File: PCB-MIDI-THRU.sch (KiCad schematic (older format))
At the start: 61 parts, among them J1 Conn_02x05_Odd_Even, J2 Conn_01x02_Male, J3 Conn_01x02_Male, J4 Conn_01x02_Male, J5 Conn_01x02_Male, J6 Conn_01x02_Male, J7 Conn_01x02_Male, U1 L7805, U2 6N136, U3 74LS14

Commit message: v0.0.1 PCB SCHEM
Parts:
- added C9: C, Capacitor_THT:C_Disc_D4.3mm_W1.9mm_P5.00mm, symbol Device:C
- C2, C3, C4, C5, C6, C7, C8: footprint (none) -> Capacitor_THT:CP_Radial_D5.0mm_P2.50mm
- U1: footprint (none) -> Package_TO_SOT_THT:TO-220-3_Horizontal_TabDown
- U2: footprint (none) -> Package_DIP:DIP-8_W7.62mm
- U3: footprint (none) -> Package_DIP:DIP-14_W7.62mm
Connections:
- net +5V: now also C9.1
- net GND: now also C9.2
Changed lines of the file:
@@
 F 0 "U2" H 3250 1975 50  0000 C CNN
 F 1 "6N136" H 3250 1884 50  0000 C CNN
-F 2 "" H 3050 1250 50  0001 L CIN
+F 2 "Package_DIP:DIP-8_W7.62mm" H 3050 1250 50  0001 L CIN
 F 3 "http://www.ti.com/lit/gpn/sn74LS14" H 3250 1550 50  0001 L CNN
 	1    3250 1550
@@
 F 0 "U3" H 5050 1967 50  0000 C CNN
 F 1 "74LS14" H 5050 1876 50  0000 C CNN
-F 2 "" H 5050 1650 50  0001 C CNN
+F 2 "Package_DIP:DIP-14_W7.62mm" H 5050 1650 50  0001 C CNN
 F 3 "http://www.ti.com/lit/gpn/sn74LS14" H 5050 1650 50  0001 C CNN
 	1    5050 1650
@@
 F 0 "U3" H 6350 2367 50  0000 C CNN
 F 1 "74LS14" H 6350 2276 50  0000 C CNN
-F 2 "" H 6350 2050 50  0001 C CNN
+F 2 "Package_DIP:DIP-14_W7.62mm" H 6350 2050 50  0001 C CNN
 F 3 "http://www.ti.com/lit/gpn/sn74LS14" H 6350 2050 50  0001 C CNN
 	2    6350 2050
@@
 F 0 "U3" H 6350 2917 50  0000 C CNN
 F 1 "74LS14" H 6350 2826 50  0000 C CNN
-F 2 "" H 6350 2600 50  0001 C CNN
+F 2 "Package_DIP:DIP-14_W7.62mm" H 6350 2600 50  0001 C CNN
 F 3 "http://www.ti.com/lit/gpn/sn74LS14" H 6350 2600 50  0001 C CNN
 	3    6350 2600
@@
 F 0 "U3" H 6350 3517 50  0000 C CNN
 F 1 "74LS14" H 6350 3426 50  0000 C CNN
-F 2 "" H 6350 3200 50  0001 C CNN
+F 2 "Package_DIP:DIP-14_W7.62mm" H 6350 3200 50  0001 C CNN
 F 3 "http://www.ti.com/lit/gpn/sn74LS14" H 6350 3200 50  0001 C CNN
 	4    6350 3200
@@
 F 0 "U3" H 6350 4117 50  0000 C CNN
 F 1 "74LS14" H 6350 4026 50  0000 C CNN
-F 2 "" H 6350 3800 50  0001 C CNN
+F 2 "Package_DIP:DIP-14_W7.62mm" H 6350 3800 50  0001 C CNN
 F 3 "http://www.ti.com/lit/gpn/sn74LS14" H 6350 3800 50  0001 C CNN
 	6    6350 3800
@@
 F 0 "U3" H 3730 4196 50  0000 L CNN
 F 1 "74LS14" H 3730 4105 50  0000 L CNN
-F 2 "" H 3500 4150 50  0001 C CNN
+F 2 "Package_DIP:DIP-14_W7.62mm" H 3500 4150 50  0001 C CNN
 F 3 "http://www.ti.com/lit/gpn/sn74LS14" H 3500 4150 50  0001 C CNN
 	7    3500 4150
@@
 F 0 "U1" H 2400 3942 50  0000 C CNN
 F 1 "L7805" H 2400 3851 50  0000 C CNN
-F 2 "" H 2425 3550 50  0001 L CIN
+F 2 "Package_TO_SOT_THT:TO-220-3_Horizontal_TabDown" H 2425 3550 50  0001 L CIN
 F 3 "http://www.st.com/content/ccc/resource/technical/document/datasheet/41/4f/b3/b0/12/d4/47/88/CD00000444.pdf/files/CD00000444.pdf/jcr:content/translations/en.CD00000444.pdf" H 2400 3650 50  0001 C CNN
 	1    2400 3700
@@
 F 0 "C2" H 2788 4096 50  0000 L CNN
 F 1 "10UF" H 2788 4005 50  0000 L CNN
-F 2 "" H 2700 4050 50  0001 C CNN
+F 2 "Capacitor_THT:CP_Radial_D5.0mm_P2.50mm" H 2700 4050 50  0001 C CNN
 F 3 "~" H 2700 4050 50  0001 C CNN
 	1    2700 4050
@@
 F 0 "U3" H 6350 4717 50  0000 C CNN
 F 1 "74LS14" H 6350 4626 50  0000 C CNN
-F 2 "" H 6350 4400 50  0001 C CNN
+F 2 "Package_DIP:DIP-14_W7.62mm" H 6350 4400 50  0001 C CNN
 F 3 "http://www.ti.com/lit/gpn/sn74LS14" H 6350 4400 50  0001 C CNN
 	5    6350 4400
@@
 F 0 "C4" V 9950 2250 50  0000 C CNN
 F 1 "10UF" V 9950 2600 50  0000 C CNN
-F 2 "" H 10000 2400 50  0001 C CNN
+F 2 "Capacitor_THT:CP_Radial_D5.0mm_P2.50mm" H 10000 2400 50  0001 C CNN
 F 3 "~" H 10000 2400 50  0001 C CNN
 	1    10000 2400
@@
 F 0 "C5" V 9950 2800 50  0000 C CNN
 F 1 "10UF" V 9950 3150 50  0000 C CNN
-F 2 "" H 10000 2950 50  0001 C CNN
+F 2 "Capacitor_THT:CP_Radial_D5.0mm_P2.50mm" H 10000 2950 50  0001 C CNN
 F 3 "~" H 10000 2950 50  0001 C CNN
 	1    10000 2950
@@
 F 0 "C6" V 9950 3450 50  0000 C CNN
 F 1 "10UF" V 9950 3800 50  0000 C CNN
-F 2 "" H 10000 3600 50  0001 C CNN
+F 2 "Capacitor_THT:CP_Radial_D5.0mm_P2.50mm" H 10000 3600 50  0001 C CNN
 F 3 "~" H 10000 3600 50  0001 C CNN
 	1    10000 3600
@@
 F 0 "C7" V 9950 4000 50  0000 C CNN
 F 1 "10UF" V 9950 4350 50  0000 C CNN
-F 2 "" H 10000 4150 50  0001 C CNN
+F 2 "Capacitor_THT:CP_Radial_D5.0mm_P2.50mm" H 10000 4150 50  0001 C CNN
 F 3 "~" H 10000 4150 50  0001 C CNN
 	1    10000 4150
@@
 F 0 "C8" V 9950 4600 50  0000 C CNN
 F 1 "10UF" V 9950 4950 50  0000 C CNN
-F 2 "" H 10000 4750 50  0001 C CNN
+F 2 "Capacitor_THT:CP_Radial_D5.0mm_P2.50mm" H 10000 4750 50  0001 C CNN
 F 3 "~" H 10000 4750 50  0001 C CNN
 	1    10000 4750
@@
 F 0 "C3" V 5600 2200 50  0000 C CNN
 F 1 "10UF" V 5600 2550 50  0000 C CNN
-F 2 "" H 5650 2350 50  0001 C CNN
+F 2 "Capacitor_THT:CP_Radial_D5.0mm_P2.50mm" H 5650 2350 50  0001 C CNN
 F 3 "~" H 5650 2350 50  0001 C CNN
 	1    5650 2350
@@
 Text Notes 7500 6800 0    50   ~ 0
 MIDI THRU V0.0.1
+$Comp
+L Device:C C9
+U 1 1 60331913
+P 4150 4150
+F 0 "C9" H 4265 4196 50  0000 L CNN
+F 1 "C" H 4265 4105 50  0000 L CNN
+F 2 "Capacitor_THT:C_Disc_D4.3mm_W1.9mm_P5.00mm" H 4188 4000 50  0001 C CNN
+F 3 "~" H 4150 4150 50  0001 C CNN
+	1    4150 4150
+	1    0    0    -1
+$EndComp
+Wire Wire Line
+	4150 3650 4150 4000
+Wire Wire Line
+	3500 3650 4150 3650
+Connection ~ 3500 3650
+Wire Wire Line
+	3500 4650 4150 4650
+Wire Wire Line
+	4150 4650 4150 4300
+Connection ~ 3500 4650
 $EndSCHEMATC

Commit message: v0.0.1 Front
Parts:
- C9: value C -> 0.1uf
- D10, D11, D5, D7, D8, D9: value 1N4001 -> 1N4148
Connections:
- net at D1.1 (K), U1.1 (IN): now also C1.1, D2.1 (K)
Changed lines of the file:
@@
 $EndComp
 Wire Wire Line
-	1900 3700 2100 3700
+	1900 3700 2050 3700
 Wire Wire Line
 	2700 3700 2900 3700
@@
 	2200 3300 2050 3300
 Wire Wire Line
-	2050 3300 2050 3950
+	2050 3300 2050 3700
 Wire Wire Line
 	2700 4150 2400 4150
@@
 P 8950 2350
 F 0 "D7" H 8850 2300 50  0000 C CNN
-F 1 "1N4001" H 9150 2400 50  0000 C CNN
+F 1 "1N4148" H 9150 2400 50  0000 C CNN
 F 2 "Diode_THT:D_A-405_P10.16mm_Horizontal" H 8950 2225 50  0001 C CNN
 F 3 "~" H 8950 2350 50  0001 C CNN
@@
 P 8950 2900
 F 0 "D8" H 8850 2850 50  0000 C CNN
-F 1 "1N4001" H 9150 2950 50  0000 C CNN
+F 1 "1N4148" H 9150 2950 50  0000 C CNN
 F 2 "Diode_THT:D_A-405_P10.16mm_Horizontal" H 8950 2775 50  0001 C CNN
 F 3 "~" H 8950 2900 50  0001 C CNN
@@
 P 8950 3550
 F 0 "D9" H 8850 3500 50  0000 C CNN
-F 1 "1N4001" H 9150 3600 50  0000 C CNN
+F 1 "1N4148" H 9150 3600 50  0000 C CNN
 F 2 "Diode_THT:D_A-405_P10.16mm_Horizontal" H 8950 3425 50  0001 C CNN
 F 3 "~" H 8950 3550 50  0001 C CNN
@@
 P 8950 4100
 F 0 "D10" H 8850 4050 50  0000 C CNN
-F 1 "1N4001" H 9150 4150 50  0000 C CNN
+F 1 "1N4148" H 9150 4150 50  0000 C CNN
 F 2 "Diode_THT:D_A-405_P10.16mm_Horizontal" H 8950 3975 50  0001 C CNN
 F 3 "~" H 8950 4100 50  0001 C CNN
@@
 P 8950 4700
 F 0 "D11" H 8850 4650 50  0000 C CNN
-F 1 "1N4001" H 9150 4750 50  0000 C CNN
+F 1 "1N4148" H 9150 4750 50  0000 C CNN
 F 2 "Diode_THT:D_A-405_P10.16mm_Horizontal" H 8950 4575 50  0001 C CNN
 F 3 "~" H 8950 4700 50  0001 C CNN
@@
 P 4600 2300
 F 0 "D5" H 4500 2250 50  0000 C CNN
-F 1 "1N4001" H 4800 2350 50  0000 C CNN
+F 1 "1N4148" H 4800 2350 50  0000 C CNN
 F 2 "Diode_THT:D_A-405_P10.16mm_Horizontal" H 4600 2175 50  0001 C CNN
 F 3 "~" H 4600 2300 50  0001 C CNN
@@
 P 4150 4150
 F 0 "C9" H 4265 4196 50  0000 L CNN
-F 1 "C" H 4265 4105 50  0000 L CNN
+F 1 "0.1uf" H 4265 4105 50  0000 L CNN
 F 2 "Capacitor_THT:C_Disc_D4.3mm_W1.9mm_P5.00mm" H 4188 4000 50  0001 C CNN
 F 3 "~" H 4150 4150 50  0001 C CNN
@@
 	4150 4650 4150 4300
 Connection ~ 3500 4650
+Connection ~ 2050 3700
+Wire Wire Line
+	2050 3700 2100 3700
+Wire Wire Line
+	2050 3700 2050 3950
 $EndSCHEMATC

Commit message: Fixed PCB up to v0.0.2
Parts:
- U2: symbol Isolator:6N136 -> Isolator:6N137
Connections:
- net GND: now also U2.5 (GND)
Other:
- note added: "MIDI THRU V0.0.2"
- note removed: "MIDI THRU V0.0.1"
- moved on the sheet: D3, J2, R1
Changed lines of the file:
@@
 $EndDescr
 $Comp
-L Isolator:6N136 U2
+L Isolator:6N137 U2
 U 1 1 6029764D
 P 3250 1550
@@
 L Device:R R1
 U 1 1 6029B749
-P 2800 1450
-F 0 "R1" V 2593 1450 50  0000 C CNN
-F 1 "220R" V 2684 1450 50  0000 C CNN
-F 2 "Resistor_THT:R_Axial_DIN0207_L6.3mm_D2.5mm_P10.16mm_Horizontal" V 2730 1450 50  0001 C CNN
-F 3 "~" H 2800 1450 50  0001 C CNN
-	1    2800 1450
-	0    1    1    0
-$EndComp
-Wire Wire Line
-	2650 1450 1500 1450
-Wire Wire Line
-	1500 1250 2000 1250
-Wire Wire Line
-	2000 1250 2000 1650
-Wire Wire Line
-	2000 1650 2950 1650
-Wire Wire Line
-	2950 1450 2950 1100
-Connection ~ 2950 1450
-Wire Wire Line
-	2000 1250 2000 1100
-Wire Wire Line
-	2000 1100 2300 1100
-Connection ~ 2000 1250
+P 2800 1550
+F 0 "R1" V 2593 1550 50  0000 C CNN
+F 1 "220R" V 2684 1550 50  0000 C CNN
+F 2 "Resistor_THT:R_Axial_DIN0207_L6.3mm_D2.5mm_P10.16mm_Horizontal" V 2730 1550 50  0001 C CNN
+F 3 "~" H 2800 1550 50  0001 C CNN
+	1    2800 1550
+	0    1    1    0
+$EndComp
+Wire Wire Line
+	2650 1550 1500 1550
+Wire Wire Line
+	1500 1350 2000 1350
+Wire Wire Line
+	2000 1350 2000 1750
+Wire Wire Line
+	2000 1750 2950 1750
+Wire Wire Line
+	2000 1350 2000 1200
+Wire Wire Line
+	2000 1200 2300 1200
+Connection ~ 2000 1350
 $Comp
 L Device:D D3
 U 1 1 6029D0DB
-P 2450 1100
-F 0 "D3" H 2450 883 50  0000 C CNN
-F 1 "D" H 2450 974 50  0000 C CNN
-F 2 "Diode_THT:D_A-405_P10.16mm_Horizontal" H 2450 975 50  0001 C CNN
-F 3 "~" H 2450 1100 50  0001 C CNN
-	1    2450 1100
-	-1   0    0    1
-$EndComp
-Wire Wire Line
-	2600 1100 2950 1100
+P 2450 1200
+F 0 "D3" H 2450 983 50  0000 C CNN
+F 1 "D" H 2450 1074 50  0000 C CNN
+F 2 "Diode_THT:D_A-405_P10.16mm_Horizontal" H 2450 1075 50  0001 C CNN
+F 3 "~" H 2450 1200 50  0001 C CNN
+	1    2450 1200
+	-1   0    0    1
+$EndComp
+Wire Wire Line
+	2600 1200 2950 1200
 $Comp
 L Device:R R2
@@
 L Connector:Conn_01x02_Male J2
 U 1 1 602F32AE
-P 1300 1250
-F 0 "J2" H 1408 1431 50  0000 C CNN
-F 1 "Conn_01x02_Male" H 1408 1340 50  0000 C CNN
-F 2 "Connector_PinHeader_2.54mm:PinHeader_1x02_P2.54mm_Vertical" H 1300 1250 50  0001 C CNN
-F 3 "~" H 1300 1250 50  0001 C CNN
-	1    1300 1250
-	1    0    0    -1
-$EndComp
-Wire Wire Line
-	1500 1450 1500 1350
+P 1300 1350
+F 0 "J2" H 1408 1531 50  0000 C CNN
+F 1 "Conn_01x02_Male" H 1408 1440 50  0000 C CNN
+F 2 "Connector_PinHeader_2.54mm:PinHeader_1x02_P2.54mm_Vertical" H 1300 1350 50  0001 C CNN
+F 3 "~" H 1300 1350 50  0001 C CNN
+	1    1300 1350
+	1    0    0    -1
+$EndComp
+Wire Wire Line
+	1500 1550 1500 1450
 $Comp
 L Connector:Conn_01x02_Male J3
@@
 Connection ~ 2700 4150
 Text Notes 7500 6800 0    50   ~ 0
-MIDI THRU V0.0.1
+MIDI THRU V0.0.2
 $Comp
 L Device:C C9
@@
 Wire Wire Line
 	2050 3700 2050 3950
+$Comp
+L power:GND #PWR?
+U 1 1 61F73DE1
+P 3550 1750
+F 0 "#PWR?" H 3550 1500 50  0001 C CNN
+F 1 "GND" H 3555 1577 50  0000 C CNN
+F 2 "" H 3550 1750 50  0001 C CNN
+F 3 "" H 3550 1750 50  0001 C CNN
+	1    3550 1750
+	1    0    0    -1
+$EndComp
+Wire Wire Line
+	2950 1200 2950 1550
+Connection ~ 2950 1550
+Wire Wire Line
+	3550 1650 3550 1550
+Wire Wire Line
+	8150 6750 8100 6750
 $EndSCHEMATC

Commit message: Removed input LED from SCH
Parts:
- removed C3: 10UF, Capacitor_THT:CP_Radial_D5.0mm_P2.50mm, symbol Device:CP_Small
- removed D5: 1N4148, Diode_THT:D_A-405_P10.16mm_Horizontal, symbol Device:D
- removed D6: LED, LED_THT:LED_D5.0mm, symbol Device:LED
- removed R4, R7: LINK, Resistor_THT:R_Axial_DIN0207_L6.3mm_D2.5mm_P10.16mm_Horizontal, symbol Device:R
- removed R5: 4K7, Resistor_THT:R_Axial_DIN0207_L6.3mm_D2.5mm_P10.16mm_Horizontal, symbol Device:R
- removed R6: 470R, Resistor_THT:R_Axial_DIN0207_L6.3mm_D2.5mm_P10.16mm_Horizontal, symbol Device:R
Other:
- note added: "MIDI THRU V0.0.3"
- note removed: "MIDI THRU V0.0.2"
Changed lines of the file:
@@
 $EndComp
-Wire Wire Line
-	3750 1650 4550 1650
-Wire Wire Line
-	5350 1650 5400 1650
 Wire Wire Line
 	6050 1650 6050 2050
@@
 Connection ~ 6650 4400
 $Comp
-L Device:R R5
-U 1 1 60327450
-P 4950 2150
-F 0 "R5" V 4850 2150 50  0000 C CNN
-F 1 "4K7" V 4950 2150 50  0000 C CNN
-F 2 "Resistor_THT:R_Axial_DIN0207_L6.3mm_D2.5mm_P10.16mm_Horizontal" V 4880 2150 50  0001 C CNN
-F 3 "~" H 4950 2150 50  0001 C CNN
-	1    4950 2150
-	0    1    1    0
-$EndComp
-$Comp
-L Device:R R6
-U 1 1 6032745A
-P 5300 2150
-F 0 "R6" V 5200 2150 50  0000 C CNN
-F 1 "470R" V 5300 2150 50  0000 C CNN
-F 2 "Resistor_THT:R_Axial_DIN0207_L6.3mm_D2.5mm_P10.16mm_Horizontal" V 5230 2150 50  0001 C CNN
-F 3 "~" H 5300 2150 50  0001 C CNN
-	1    5300 2150
-	0    1    1    0
-$EndComp
-$Comp
-L Device:CP_Small C3
-U 1 1 60327464
-P 5650 2350
-F 0 "C3" V 5600 2200 50  0000 C CNN
-F 1 "10UF" V 5600 2550 50  0000 C CNN
-F 2 "Capacitor_THT:CP_Radial_D5.0mm_P2.50mm" H 5650 2350 50  0001 C CNN
-F 3 "~" H 5650 2350 50  0001 C CNN
-	1    5650 2350
-	0    -1   -1   0
-$EndComp
-$Comp
-L Device:D D5
-U 1 1 6032746E
-P 4600 2300
-F 0 "D5" H 4500 2250 50  0000 C CNN
-F 1 "1N4148" H 4800 2350 50  0000 C CNN
-F 2 "Diode_THT:D_A-405_P10.16mm_Horizontal" H 4600 2175 50  0001 C CNN
-F 3 "~" H 4600 2300 50  0001 C CNN
-	1    4600 2300
-	1    0    0    -1
-$EndComp
-$Comp
-L Device:LED D6
-U 1 1 60327478
-P 5600 2150
-F 0 "D6" H 5350 2100 50  0000 C CNN
-F 1 "LED" H 5600 2050 50  0000 C CNN
-F 2 "LED_THT:LED_D5.0mm" H 5600 2150 50  0001 C CNN
-F 3 "~" H 5600 2150 50  0001 C CNN
-	1    5600 2150
-	-1   0    0    1
-$EndComp
-Wire Wire Line
-	5750 2150 5750 2250
-Wire Wire Line
-	5550 2350 5150 2350
-Wire Wire Line
-	5150 2350 5150 2150
-Wire Wire Line
-	5100 2150 5150 2150
-Connection ~ 5150 2150
-Wire Wire Line
-	5150 2350 4750 2350
-Wire Wire Line
-	4750 2350 4750 2300
-Connection ~ 5150 2350
-Wire Wire Line
-	4450 2300 4450 2150
-Wire Wire Line
-	4450 2150 4550 2150
-$Comp
 L power:GND #PWR016
 U 1 1 6032E968
@@
 	10700 4650 10700 4750
 $Comp
-L Device:R R4
-U 1 1 60348119
-P 4550 1800
-F 0 "R4" V 4450 1800 50  0000 C CNN
-F 1 "LINK" V 4550 1800 50  0000 C CNN
-F 2 "Resistor_THT:R_Axial_DIN0207_L6.3mm_D2.5mm_P10.16mm_Horizontal" V 4480 1800 50  0001 C CNN
-F 3 "~" H 4550 1800 50  0001 C CNN
-	1    4550 1800
-	1    0    0    -1
-$EndComp
-Connection ~ 4550 1650
-Wire Wire Line
-	4550 1650 4750 1650
-$Comp
-L Device:R R7
-U 1 1 6034E6CD
-P 5400 1800
-F 0 "R7" V 5300 1800 50  0000 C CNN
-F 1 "LINK" V 5400 1800 50  0000 C CNN
-F 2 "Resistor_THT:R_Axial_DIN0207_L6.3mm_D2.5mm_P10.16mm_Horizontal" V 5330 1800 50  0001 C CNN
-F 3 "~" H 5400 1800 50  0001 C CNN
-	1    5400 1800
-	1    0    0    -1
-$EndComp
-Connection ~ 5400 1650
-Wire Wire Line
-	5400 1650 6050 1650
-Wire Wire Line
-	5400 1950 4550 1950
-Wire Wire Line
-	4550 1950 4550 2150
-Connection ~ 4550 1950
-Connection ~ 4550 2150
-Wire Wire Line
-	4550 2150 4800 2150
-$Comp
-L power:GND #PWR010
-U 1 1 6035A26F
-P 5750 2250
-F 0 "#PWR010" H 5750 2000 50  0001 C CNN
-F 1 "GND" V 5755 2122 50  0000 R CNN
-F 2 "" H 5750 2250 50  0001 C CNN
-F 3 "" H 5750 2250 50  0001 C CNN
-	1    5750 2250
-	0    -1   -1   0
-$EndComp
-Connection ~ 5750 2250
-Wire Wire Line
-	5750 2250 5750 2350
-$Comp
 L Device:R R3
 U 1 1 6035BA5A
@@
 Connection ~ 2700 4150
 Text Notes 7500 6800 0    50   ~ 0
-MIDI THRU V0.0.2
+MIDI THRU V0.0.3
 $Comp
 L Device:C C9
@@
 	3550 1650 3550 1550
 Wire Wire Line
-	8150 6750 8100 6750
+	3750 1650 4750 1650
+Wire Wire Line
+	5350 1650 6050 1650
 $EndSCHEMATC

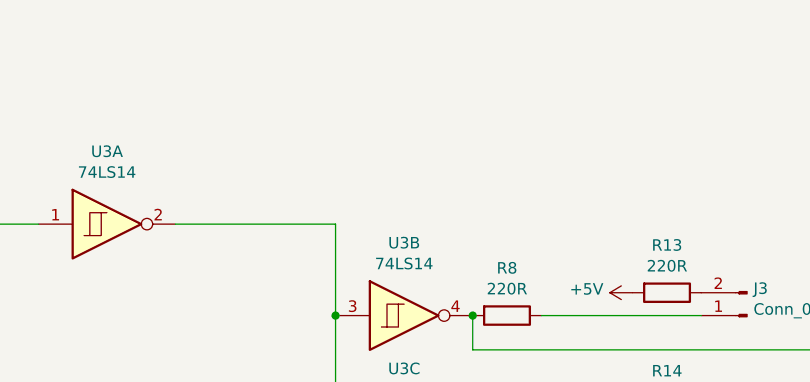
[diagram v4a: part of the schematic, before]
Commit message: Mounting holes added to sche
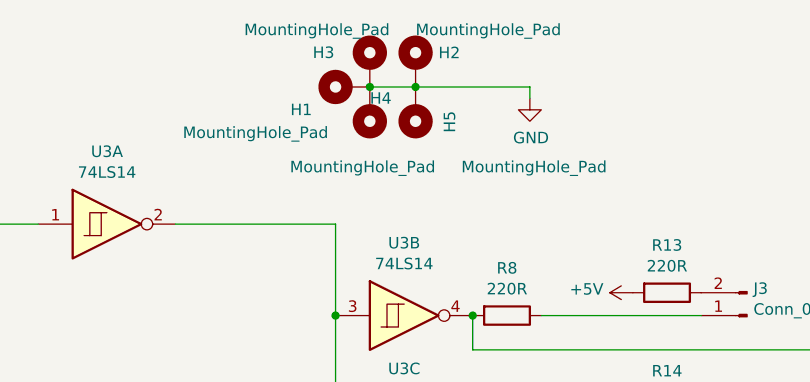
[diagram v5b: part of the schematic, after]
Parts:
- added H1: MountingHole_Pad, symbol Mechanical:MountingHole_Pad
- added H2, H3, H4, H5: MountingHole_Pad, MountingHole:MountingHole_3.2mm_M3_DIN965_Pad, symbol Mechanical:MountingHole_Pad
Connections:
- net GND: now also H1.1, H2.1, H3.1, H4.1, H5.1
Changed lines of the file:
@@
 	2050 3700 2050 3950
 $Comp
-L power:GND #PWR?
+L power:GND #PWR0101
 U 1 1 61F73DE1
 P 3550 1750
-F 0 "#PWR?" H 3550 1500 50  0001 C CNN
+F 0 "#PWR0101" H 3550 1500 50  0001 C CNN
 F 1 "GND" H 3555 1577 50  0000 C CNN
 F 2 "" H 3550 1750 50  0001 C CNN
@@
 Wire Wire Line
 	5350 1650 6050 1650
+$Comp
+L Mechanical:MountingHole_Pad H3
+U 1 1 61FFE19C
+P 6200 950
+F 0 "H3" H 5950 1000 50  0000 L CNN
+F 1 "MountingHole_Pad" H 5650 1100 50  0000 L CNN
+F 2 "MountingHole:MountingHole_3.2mm_M3_DIN965_Pad" H 6200 950 50  0001 C CNN
+F 3 "~" H 6200 950 50  0001 C CNN
+	1    6200 950
+	1    0    0    -1
+$EndComp
+$Comp
+L Mechanical:MountingHole_Pad H4
+U 1 1 61FFE6DE
+P 6200 1150
+F 0 "H4" H 6200 1100 50  0000 R CNN
+F 1 "MountingHole_Pad" H 6550 1400 50  0000 R CNN
+F 2 "MountingHole:MountingHole_3.2mm_M3_DIN965_Pad" H 6200 1150 50  0001 C CNN
+F 3 "~" H 6200 1150 50  0001 C CNN
+	1    6200 1150
+	-1   0    0    1
+$EndComp
+$Comp
+L Mechanical:MountingHole_Pad H2
+U 1 1 62000598
+P 6400 950
+F 0 "H2" H 6500 999 50  0000 L CNN
+F 1 "MountingHole_Pad" H 6400 1100 50  0000 L CNN
+F 2 "MountingHole:MountingHole_3.2mm_M3_DIN965_Pad" H 6400 950 50  0001 C CNN
+F 3 "~" H 6400 950 50  0001 C CNN
+	1    6400 950
+	1    0    0    -1
+$EndComp
+$Comp
+L Mechanical:MountingHole_Pad H5
+U 1 1 62000D54
+P 6400 1150
+F 0 "H5" V 6250 1250 50  0000 R CNN
+F 1 "MountingHole_Pad" H 6200 1400 50  0000 R CNN
+F 2 "MountingHole:MountingHole_3.2mm_M3_DIN965_Pad" H 6400 1150 50  0001 C CNN
+F 3 "~" H 6400 1150 50  0001 C CNN
+	1    6400 1150
+	-1   0    0    1
+$EndComp
+$Comp
+L Mechanical:MountingHole_Pad H1
+U 1 1 6200CA7D
+P 6100 1050
+F 0 "H1" V 6000 1250 50  0000 C CNN
+F 1 "MountingHole_Pad" V 5900 1450 50  0000 C CNN
+F 2 "" H 6100 1050 50  0001 C CNN
+F 3 "~" H 6100 1050 50  0001 C CNN
+	1    6100 1050
+	0    -1   -1   0
+$EndComp
+Connection ~ 6200 1050
+Wire Wire Line
+	6200 1050 6400 1050
+Connection ~ 6400 1050
+Wire Wire Line
+	6900 1050 6900 1100
+Wire Wire Line
+	6400 1050 6900 1050
+$Comp
+L power:GND #PWR?
+U 1 1 6201766C
+P 6900 1100
+F 0 "#PWR?" H 6900 850 50  0001 C CNN
+F 1 "GND" H 6905 927 50  0000 C CNN
+F 2 "" H 6900 1100 50  0001 C CNN
+F 3 "" H 6900 1100 50  0001 C CNN
+	1    6900 1100
+	1    0    0    -1
+$EndComp
 $EndSCHEMATC

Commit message: PCB minus input LED
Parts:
- H1: footprint (none) -> MountingHole:MountingHole_3.2mm_M3_DIN965_Pad
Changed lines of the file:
@@
 F 0 "H1" V 6000 1250 50  0000 C CNN
 F 1 "MountingHole_Pad" V 5900 1450 50  0000 C CNN
-F 2 "" H 6100 1050 50  0001 C CNN
+F 2 "MountingHole:MountingHole_3.2mm_M3_DIN965_Pad" H 6100 1050 50  0001 C CNN
 F 3 "~" H 6100 1050 50  0001 C CNN
 	1    6100 1050
@@
 	6400 1050 6900 1050
 $Comp
-L power:GND #PWR?
+L power:GND #PWR0102
 U 1 1 6201766C
 P 6900 1100
-F 0 "#PWR?" H 6900 850 50  0001 C CNN
+F 0 "#PWR0102" H 6900 850 50  0001 C CNN
 F 1 "GND" H 6905 927 50  0000 C CNN
 F 2 "" H 6900 1100 50  0001 C CNN

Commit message: PCB V0.0.3
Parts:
- H1: value MountingHole_Pad -> H3
- H2: value MountingHole_Pad -> H2
- H3: value MountingHole_Pad -> H1
- H4: value MountingHole_Pad -> H4
- H5: value MountingHole_Pad -> H5
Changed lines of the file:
@@
 P 6200 950
 F 0 "H3" H 5950 1000 50  0000 L CNN
-F 1 "MountingHole_Pad" H 5650 1100 50  0000 L CNN
+F 1 "H1" H 5650 1100 50  0000 L CNN
 F 2 "MountingHole:MountingHole_3.2mm_M3_DIN965_Pad" H 6200 950 50  0001 C CNN
 F 3 "~" H 6200 950 50  0001 C CNN
@@
 P 6200 1150
 F 0 "H4" H 6200 1100 50  0000 R CNN
-F 1 "MountingHole_Pad" H 6550 1400 50  0000 R CNN
+F 1 "H4" H 6550 1400 50  0000 R CNN
 F 2 "MountingHole:MountingHole_3.2mm_M3_DIN965_Pad" H 6200 1150 50  0001 C CNN
 F 3 "~" H 6200 1150 50  0001 C CNN
@@
 P 6400 950
 F 0 "H2" H 6500 999 50  0000 L CNN
-F 1 "MountingHole_Pad" H 6400 1100 50  0000 L CNN
+F 1 "H2" H 6400 1100 50  0000 L CNN
 F 2 "MountingHole:MountingHole_3.2mm_M3_DIN965_Pad" H 6400 950 50  0001 C CNN
 F 3 "~" H 6400 950 50  0001 C CNN
@@
 P 6400 1150
 F 0 "H5" V 6250 1250 50  0000 R CNN
-F 1 "MountingHole_Pad" H 6200 1400 50  0000 R CNN
+F 1 "H5" H 6200 1400 50  0000 R CNN
 F 2 "MountingHole:MountingHole_3.2mm_M3_DIN965_Pad" H 6400 1150 50  0001 C CNN
 F 3 "~" H 6400 1150 50  0001 C CNN
@@
 P 6100 1050
 F 0 "H1" V 6000 1250 50  0000 C CNN
-F 1 "MountingHole_Pad" V 5900 1450 50  0000 C CNN
+F 1 "H3" V 5900 1450 50  0000 C CNN
 F 2 "MountingHole:MountingHole_3.2mm_M3_DIN965_Pad" H 6100 1050 50  0001 C CNN
 F 3 "~" H 6100 1050 50  0001 C CNN
